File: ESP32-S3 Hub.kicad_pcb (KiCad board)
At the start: 6 copper layers, 15 x 30 mm, 69 parts, among them J1 Precidip 853-87-004-20-001101, J10 Precidip 853-87-004-20-001101, J11 7 pin FPC 0.3mm Aces 51688-00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, J12 Precidip 853-87-004-20-001101, J13 TE 3-2363961-0 receptacle, J15 Precidip 853-87-004-20-001101, J16 TE 3-2363961-0 receptacle, J18 Precidip 852-10-004-20-001101, J2 Precidip 853-87-004-20-001101, J3 7 pin FPC 0.3mm Aces 51688-00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, J4 Precidip 853-87-004-20-001101, J5 7 pin FPC 0.3mm Aces 51688-00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, J6 Precidip 853-87-004-20-001101, J7 Precidip 853-87-004-20-001101, J8 7 pin FPC 0.3mm Aces 51688-00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, J9 Precidip 853-87-004-20-001101, SW1 Mitsumi R-667996, SW2 Mitsumi R-667996, U1 ESP32-S3, U2 SN74LV595A, U3 THVD1420DRLR, U4 TPS2521ARPWR, U5 SN74LV595A, U6 TS5A3159DCK, Y1 ABM11-40.000MHZ-B1U-T3, 10ppm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

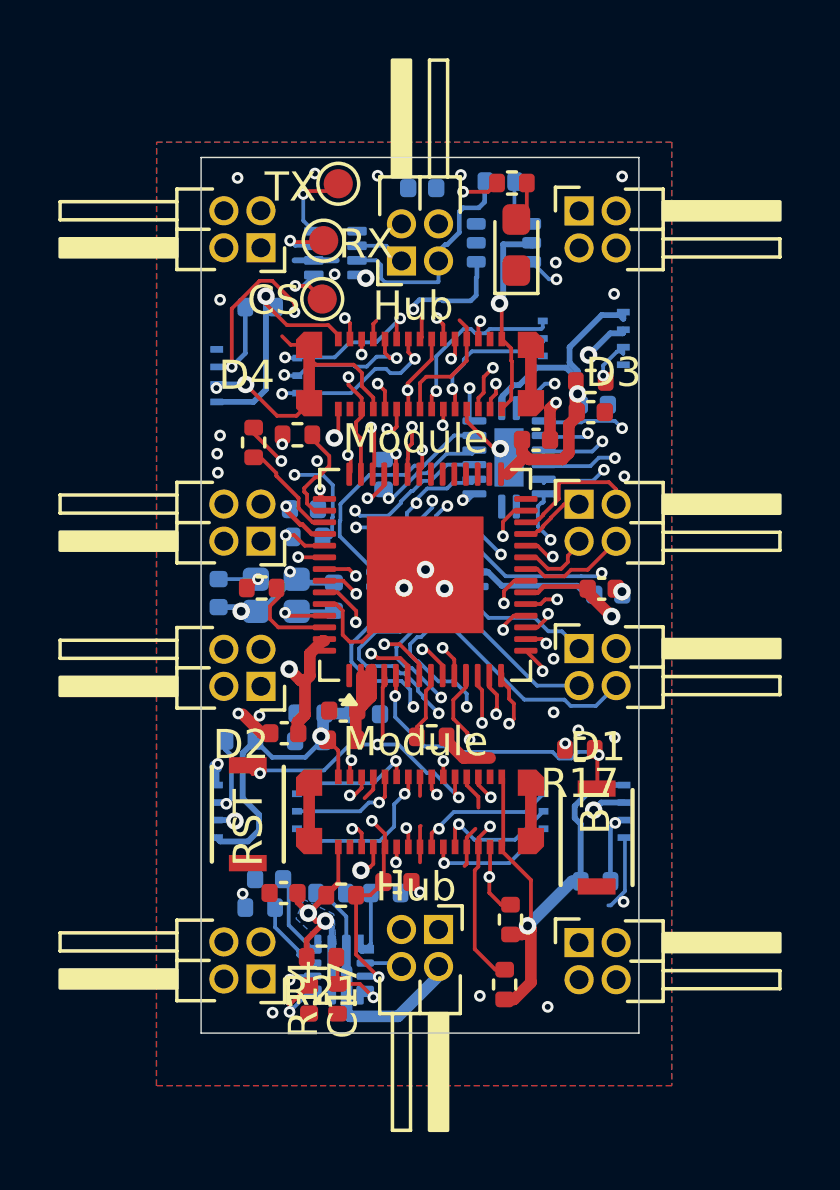
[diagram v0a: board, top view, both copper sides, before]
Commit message: Finished Reroute of ESP32-s3 hub
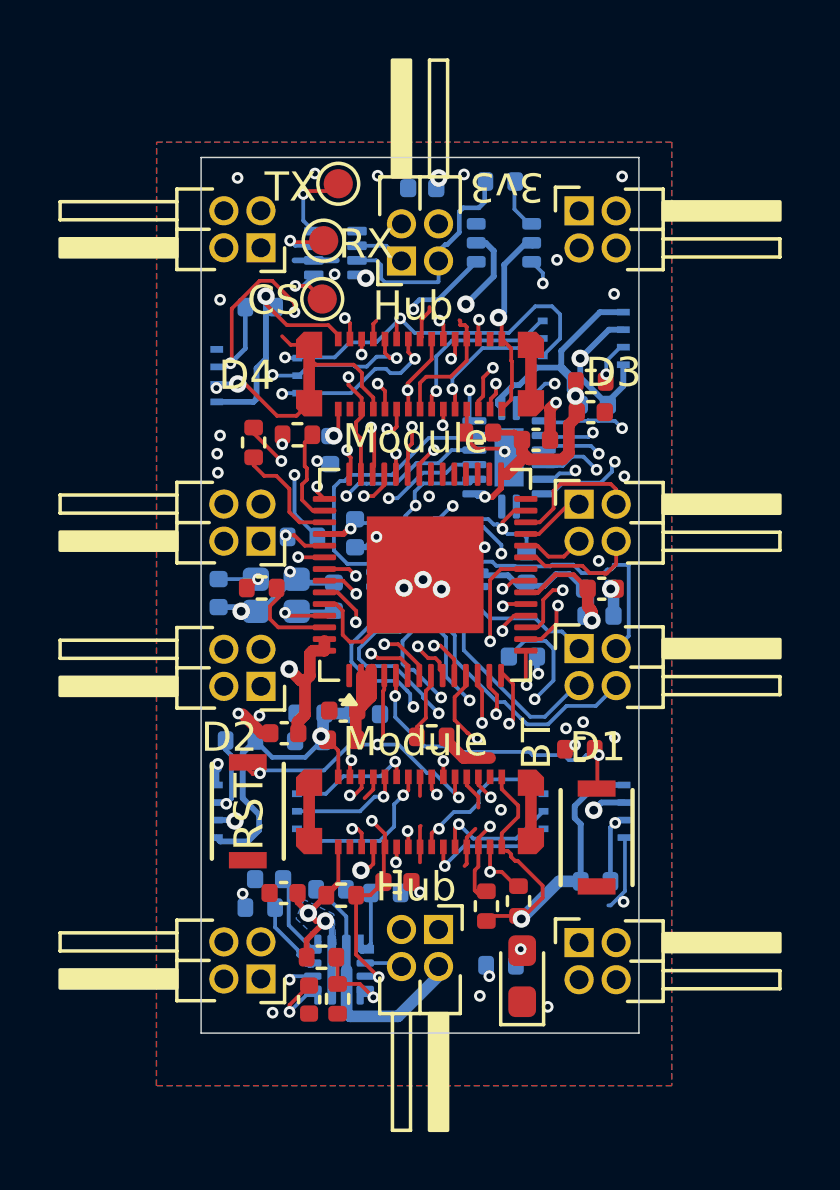
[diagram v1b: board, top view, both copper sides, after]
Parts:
- added C19: 10nF, Capacitor_SMD:C_0402_1005Metric, B.Cu at (152.3, 91.8)
- added C20: 10nF, Capacitor_SMD:C_0402_1005Metric, B.Cu at (161.6, 97.5)
- added C21: 10nF, Capacitor_SMD:C_0402_1005Metric, B.Cu at (158.9, 98.9)
- added C22: 10nF, Capacitor_SMD:C_0402_1005Metric, F.Cu at (157.4, 91.2)
- R10: moved to B.Cu
- moved R10 26.8 mm to (158.2, 109.5)
- moved D1 25.1 mm to (158.9, 109.8)
- moved R13 5.85 mm to (159.1, 95.8), turned to -90 degrees
- moved R9 2.76 mm to (157.7, 107.5)
- moved C10 1.93 mm to (153.2, 94.7), turned to -90 degrees
- moved R8 0.69 mm to (158.8, 107.3)
- moved C15 0.40 mm to (161.5, 96.6)
- moved R5 0.18 mm to (151.4, 94.8)
- moved R11 0.12 mm to (152.3, 106.9)
- moved SW2 0.10 mm to (149.5, 104.2)
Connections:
- U1 pad 18: 4CSA-D -> 4CSA-A
- U1 pad 21: 4CSA-A -> 4CSA-D
- U1 pad 22: 3CSA-D -> 4CSA-B
- U1 pad 23: 3CSA-C -> 3CSA-D
- U1 pad 24: 4CSA-B -> 3CSA-C
- U2 pad 1: 4A -> 3A
- U2 pad 15: 4B -> 3B
- U2 pad 2: 4D -> 3D
- U2 pad 3: 4C -> 3C
- U2 pad 4: 3A -> 4D
- U2 pad 5: 3B -> 4C
- U2 pad 6: 3D -> 4A
- U2 pad 7: 3C -> 4B
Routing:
- net BOOT: track 11.4 -> 32.5 mm, vias 3 -> 4
- net 4B: track 6.80 -> 26.8 mm
- net 4A: track 3.89 -> 21.8 mm
- net 4D: track 7.93 -> 25.1 mm, vias 2 -> 1
- net ShiftEn: track 6.62 -> 23.7 mm, vias 3 -> 2
- net 4C: track 7.02 -> 23.5 mm
- net GND: track 58.0 -> 72.1 mm, vias 40 -> 45
- net ShiftCLK: track 5.06 -> 17.4 mm
- net CS1: track 19.2 -> 31.4 mm, vias 2 -> 3
- net 4CSA-B: track 13.6 -> 23.4 mm
- net MOSI1: track 44.7 -> 54.0 mm
- net ShiftLatch: track 7.54 -> 16.6 mm
- net 4CSA-A: track 12.4 -> 20.0 mm
- net 4CSA-D: track 16.3 -> 23.3 mm
- net 4CSA-C: track 14.3 -> 21.0 mm
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
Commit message: Revised routing according to new labels and components
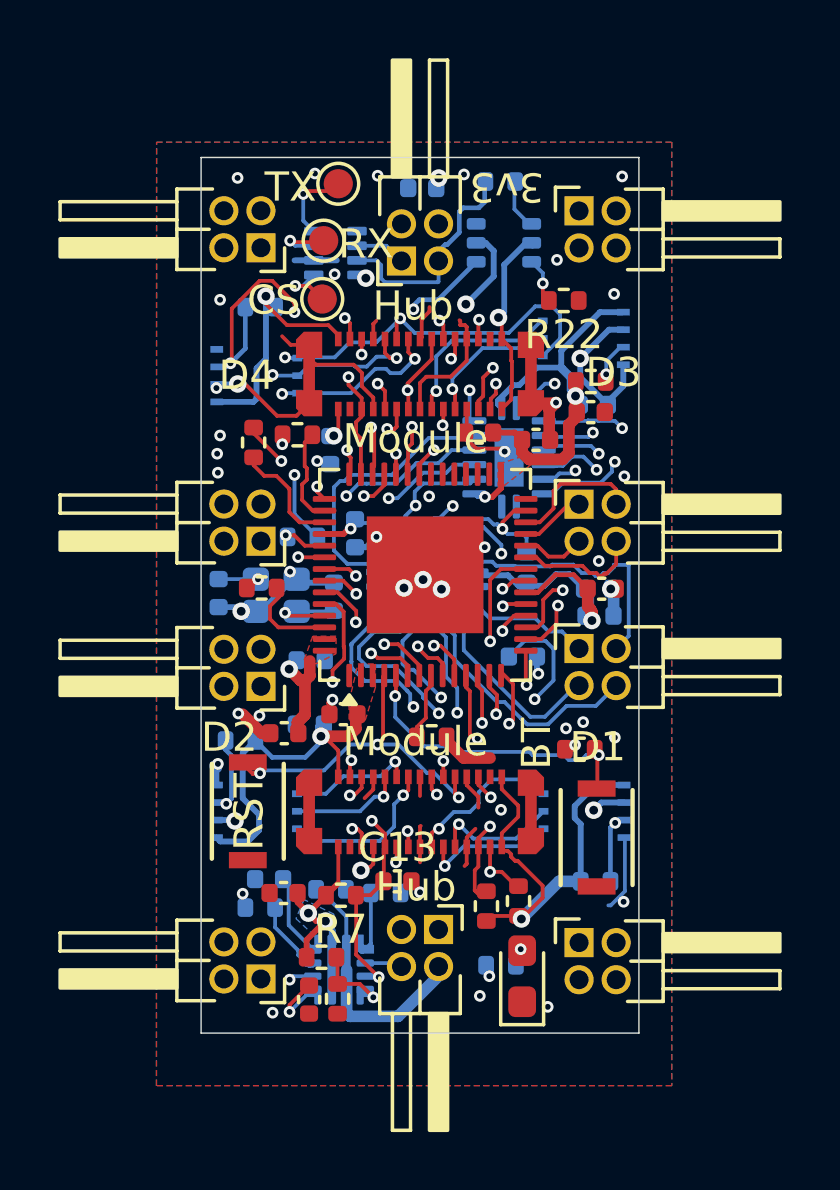
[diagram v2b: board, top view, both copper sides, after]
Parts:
- removed C3: 0.1uF, Capacitor_SMD:C_0402_1005Metric
- removed FB1: 120ohm imp @100mhz, 1 amp, Inductor_SMD:L_0402_1005Metric
- added R22: 10k, Resistor_SMD:R_0402_1005Metric, F.Cu at (160.3, 86.7)
- C10, C4, C5, C6, C8: value 0.1uF -> 100nF
- J11, J3, J5, J8: value 7 pin FPC 0.3mm Aces 51688-0070M-001 -> FPC 0.3mm Aces 51688-0070M
- R10: value 80.6 ohm -> 100 ohm
- TP20: value CS0 -> RTS
- U1: value ESP32-S3 -> ESP32-S3 FN8
- Y1: value ABM11-40.000MHZ-B1U-T3, 10ppm, 10pF -> 2 pin 40MHZ, 10ppm tol., 20ppm stab., 10pF
- moved C6 2.65 mm to (151.7, 99.0)
- moved C2 0.38 mm to (151.6, 101.2)
- moved C4 0.13 mm to (152.8, 100.9)
- turned C11 to 90 degrees
- turned C5 to 180 degrees
- turned C7 to 180 degrees
- turned C8 to 180 degrees
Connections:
- net 1A renamed PWM-1A
- net 1B renamed PWM-1B
- net 1C renamed PWM-1C
- net 1CSA-A renamed ADC-1A
- net 1CSA-B renamed ADC-1B
- net 1CSA-C renamed ADC-1C
- net 1CSA-D renamed ADC-1D
- net 1D renamed PWM-1D
- net 2A renamed PWM-2A
- net 2B renamed PWM-2B
- net 2C renamed PWM-2C
- net 2CSA-A renamed ADC-2A
- net 2CSA-B renamed ADC-2B
- net 2CSA-C renamed ADC-2C
- net 2CSA-D renamed ADC-2D
- net 2D renamed PWM-2D
- net 3A renamed PWM-3A
- net 3B renamed PWM-3B
- net 3C renamed PWM-3C
- net 3CSA-A renamed ADC-3A
- net 3CSA-B renamed ADC-3B
- net 3CSA-C renamed ADC-3C
- net 3CSA-D renamed ADC-3D
- net 3D renamed PWM-3D
- net 4A renamed PWM-4A
- net 4B renamed PWM-4B
- net 4C renamed PWM-4C
- net 4CSA-A renamed ADC-4A
- net 4CSA-B renamed ADC-4B
- net 4CSA-C renamed ADC-4C
- net 4CSA-D renamed ADC-4D
- net 4D renamed PWM-4D
- net CS1 renamed CS-1
- net CS2 renamed CS-2
- net CS3 renamed CS-3
- net CS4 renamed CS-4
- net Free1 renamed Free-1
- net Free2 renamed Free-2
- net MISO1 renamed MISO
- net MOSI1 renamed MOSI
- net SCK1 renamed SCK
- net SCL1 renamed SCL
- net SDA1 renamed SDA
- net UART0-RTS/CS0 renamed UART0-RTS
- C11 pad 1: Net-(C11-Pad1) -> GND
- C11 pad 2: GND -> Net-(C11-Pad2)
- C4 pad 1: Net-(C4-Pad1) -> VDD
- C5 pad 1: VDD -> GND
- C5 pad 2: GND -> VDD
- C7 pad 1: VDD -> GND
- C7 pad 2: GND -> VDD
- C8 pad 1: VDD -> GND
- C8 pad 2: GND -> VDD
- R6 pad 1: Net-(C11-Pad1) -> Net-(C11-Pad2)
- U1 pad 2: Net-(C4-Pad1) -> VDD
- U1 pad 3: Net-(C4-Pad1) -> VDD
- U1 pad 52: GND -> R_Switch
- U6 pad 6: BOOT -> R_Switch
- Y1 pad 3: Net-(C11-Pad1) -> Net-(C11-Pad2)
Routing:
- net R_Switch: track 0.00 -> 31.8 mm, vias 0 -> 3
- net BOOT: track 32.5 -> 10.3 mm, vias 4 -> 2
- net Net-(C4-Pad1): track 3.88 -> 0.00 mm
- net GND: track 72.1 -> 68.9 mm, vias 45 -> 46
- net VDD: track 89.9 -> 88.0 mm
- net Net-(C11-Pad2): track 0.00 -> 1.76 mm, vias 0 -> 1
- net Net-(C11-Pad1): track 1.76 -> 0.00 mm, vias 1 -> 0
- net SCL: track 36.1 -> 36.6 mm
- net CS-1: track 31.4 -> 30.8 mm
- added copper zone on F.Cu, net VDD

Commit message: Decreased number of wires on power plane for more continuous signal
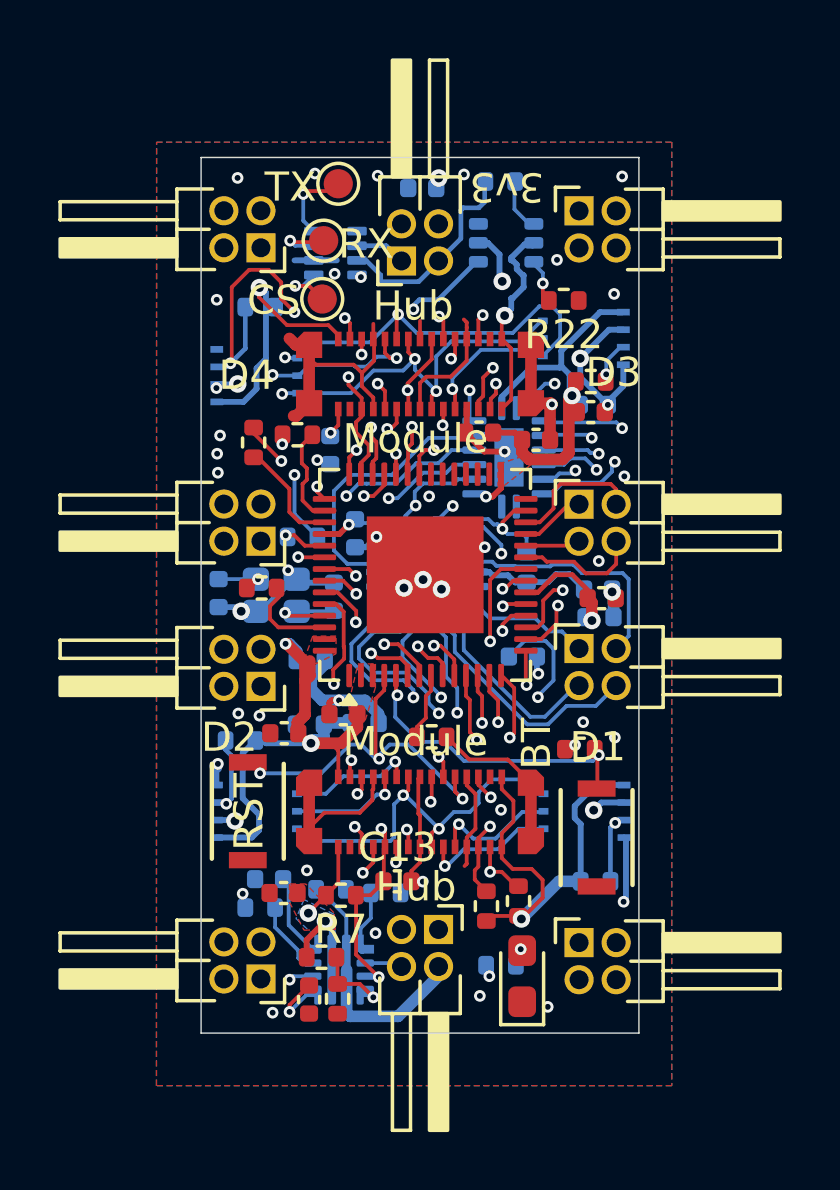
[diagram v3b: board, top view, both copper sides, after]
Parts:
- added C3: 10uF, Capacitor_SMD:C_0402_1005Metric, B.Cu at (153.5, 101.2)
- moved C8 0.33 mm to (161.6, 96.9)
- moved U6 0.07 mm to (158.3, 84.7)
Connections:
- J12 pad 4: VBUS -> VDD
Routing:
- net VBUS: track 38.8 -> 8.99 mm
- net GND: track 68.9 -> 84.6 mm
- net MOSI: track 54.0 -> 60.4 mm
- net CS-2: track 24.8 -> 31.0 mm, vias 2 -> 4
- net SCL: track 36.6 -> 40.8 mm
- net NRST: track 42.5 -> 46.4 mm
- net SDA: track 38.4 -> 41.0 mm
- net MISO: track 46.0 -> 48.4 mm
- net VDD: track 88.0 -> 86.1 mm
- net UART0_RX: track 34.4 -> 35.9 mm
- net UART0_TX: track 45.3 -> 43.9 mm
- net CS-1: track 30.8 -> 29.5 mm
- net LED: track 25.4 -> 24.3 mm
- net PWM-2B: track 21.2 -> 20.5 mm
- net SCK: track 45.1 -> 45.8 mm
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
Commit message: Added shielding vias all around edge
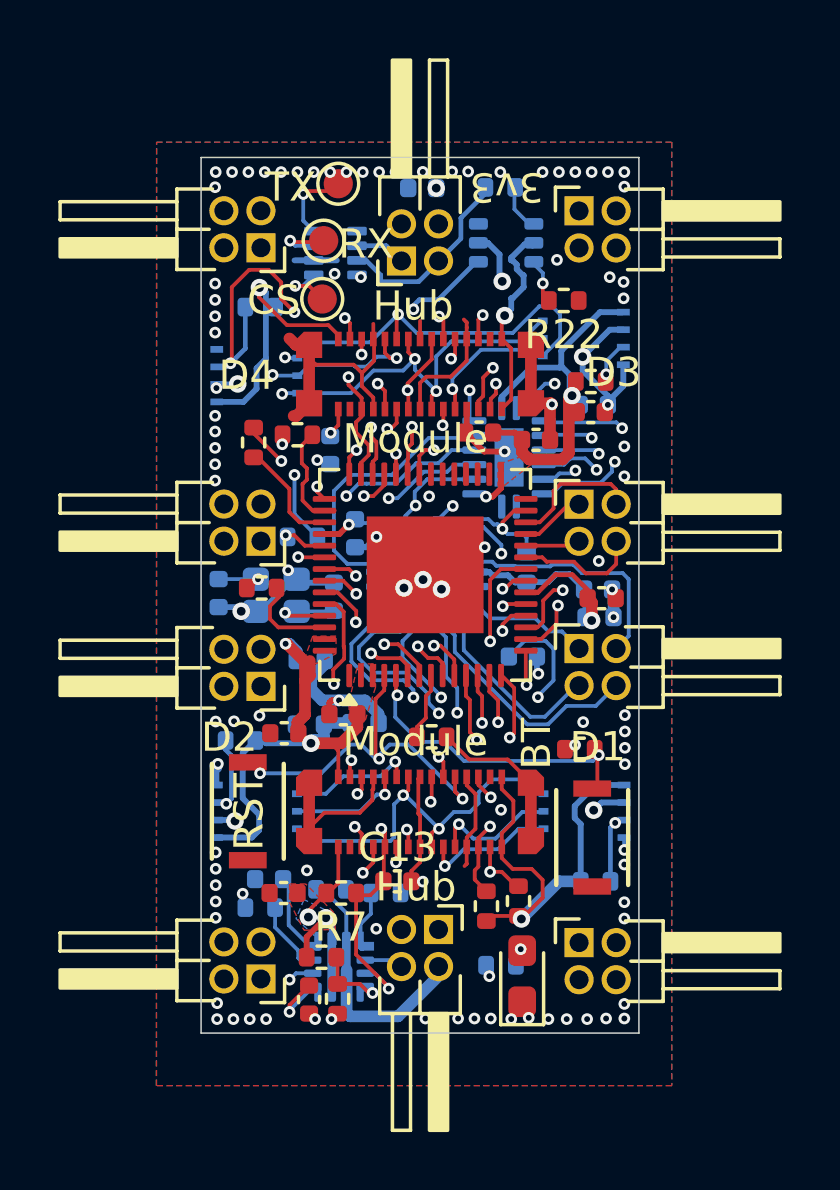
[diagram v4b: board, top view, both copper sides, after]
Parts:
- moved R16 0.20 mm to (158.2, 82.8)
- moved SW1 0.15 mm to (161.3, 105.1)
- moved U4 0.10 mm to (152.6, 109.5)
- moved R7 0.08 mm to (152.7, 107.0)
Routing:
- net GND: track 84.6 -> 82.8 mm, vias 46 -> 103
- net NRST: track 46.4 -> 47.6 mm
- net PWM-3C: track 9.29 -> 8.77 mm
- net RS485+: track 36.3 -> 35.8 mm

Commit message: Fixed silkscreen and traces according to DRC
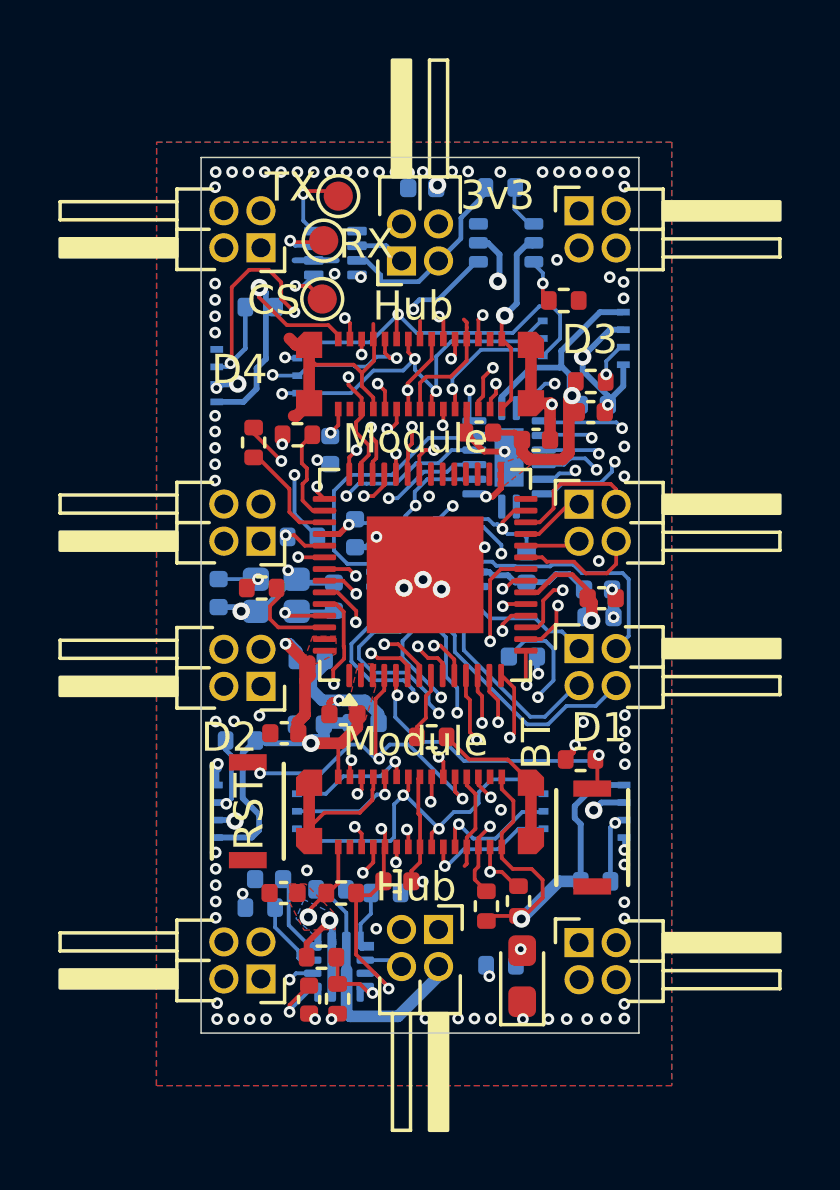
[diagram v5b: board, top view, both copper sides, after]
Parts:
- moved TP3 0.42 mm to (152.6, 83.1)
- moved R17 0.35 mm to (160.9, 102.4)

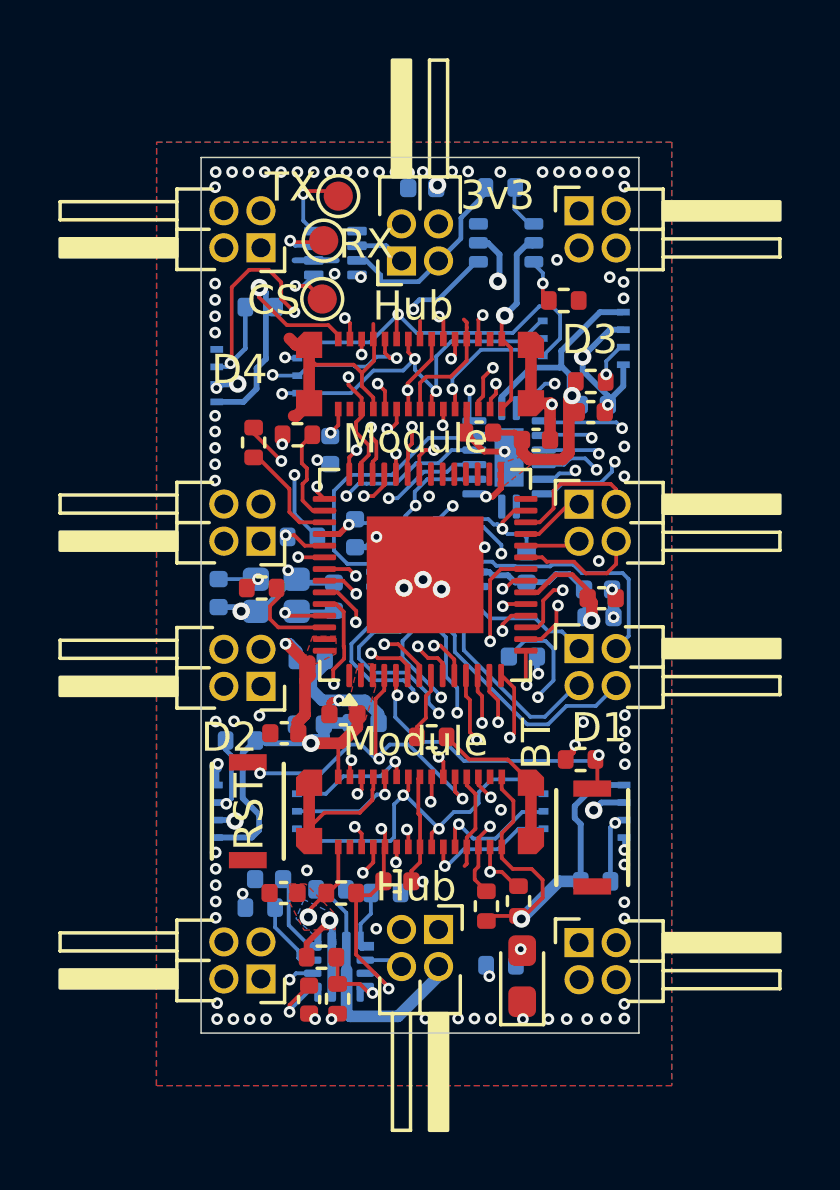
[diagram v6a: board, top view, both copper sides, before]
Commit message: Updated 3D models
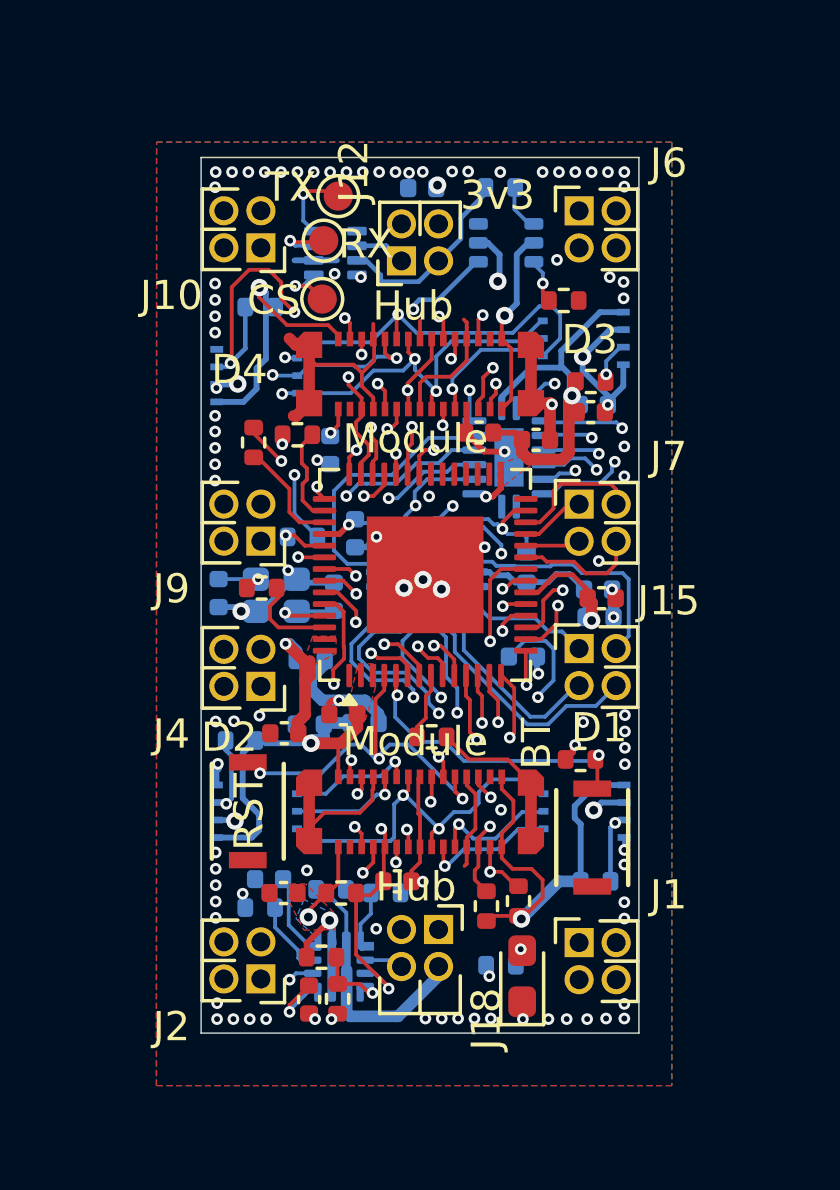
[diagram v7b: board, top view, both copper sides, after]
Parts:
- J1, J10, J12, J15, J2, J4, J6, J7, J9: footprint Connector_PinHeader_1.27mm:PinHeader_2x02_P1.27mm_Horizontal -> custom_Connector:Precidip 853-87-004-20-001101
- J18: footprint Connector_PinHeader_1.27mm:PinHeader_2x02_P1.27mm_Horizontal -> custom_Connector:Precidip 852-10-004-20-001101
